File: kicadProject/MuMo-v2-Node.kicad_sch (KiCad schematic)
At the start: 75 parts, among them Q1 PJC7400, SW1 Reset, U1 MCP73123, U2 LoRa-E5, U3 CP2102N, U4 eInk_Display_1.54"200x200px, U5 BME680, U6 TSL25911, U7 BR24G512FVT-5AE2, U8 BR24G512FVT-5AE2

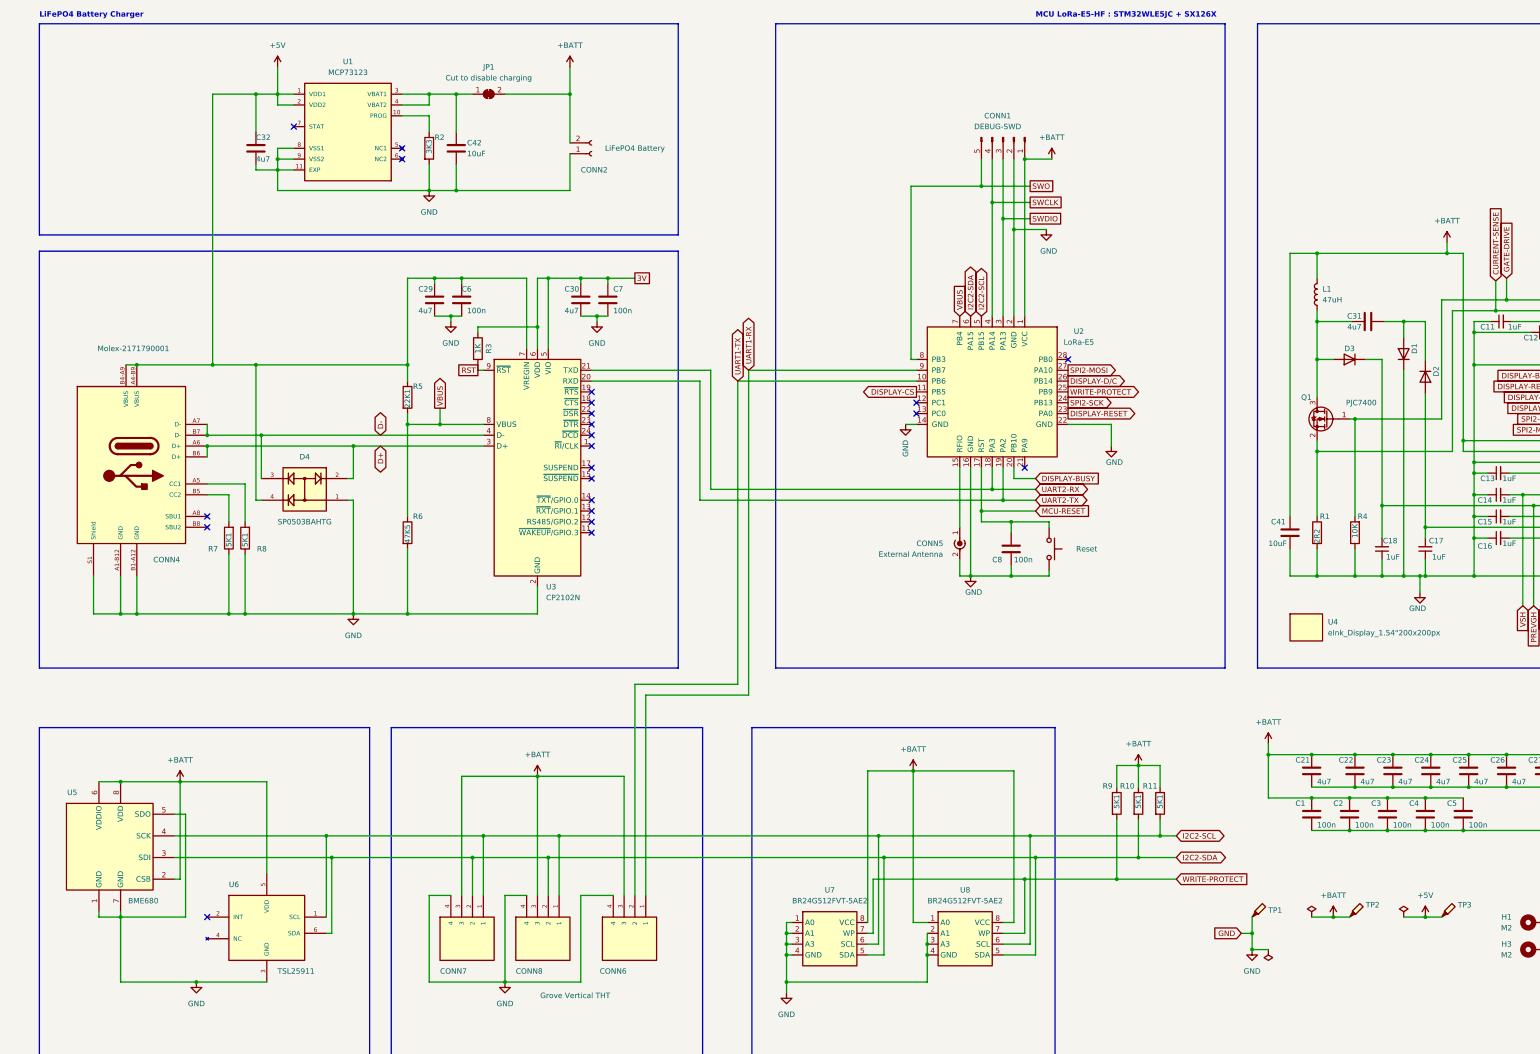
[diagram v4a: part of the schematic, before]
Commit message: V2.4
Updated to Kicad V7
* small design improvements, resolving the DRC of V7
* ready for production at Aisler
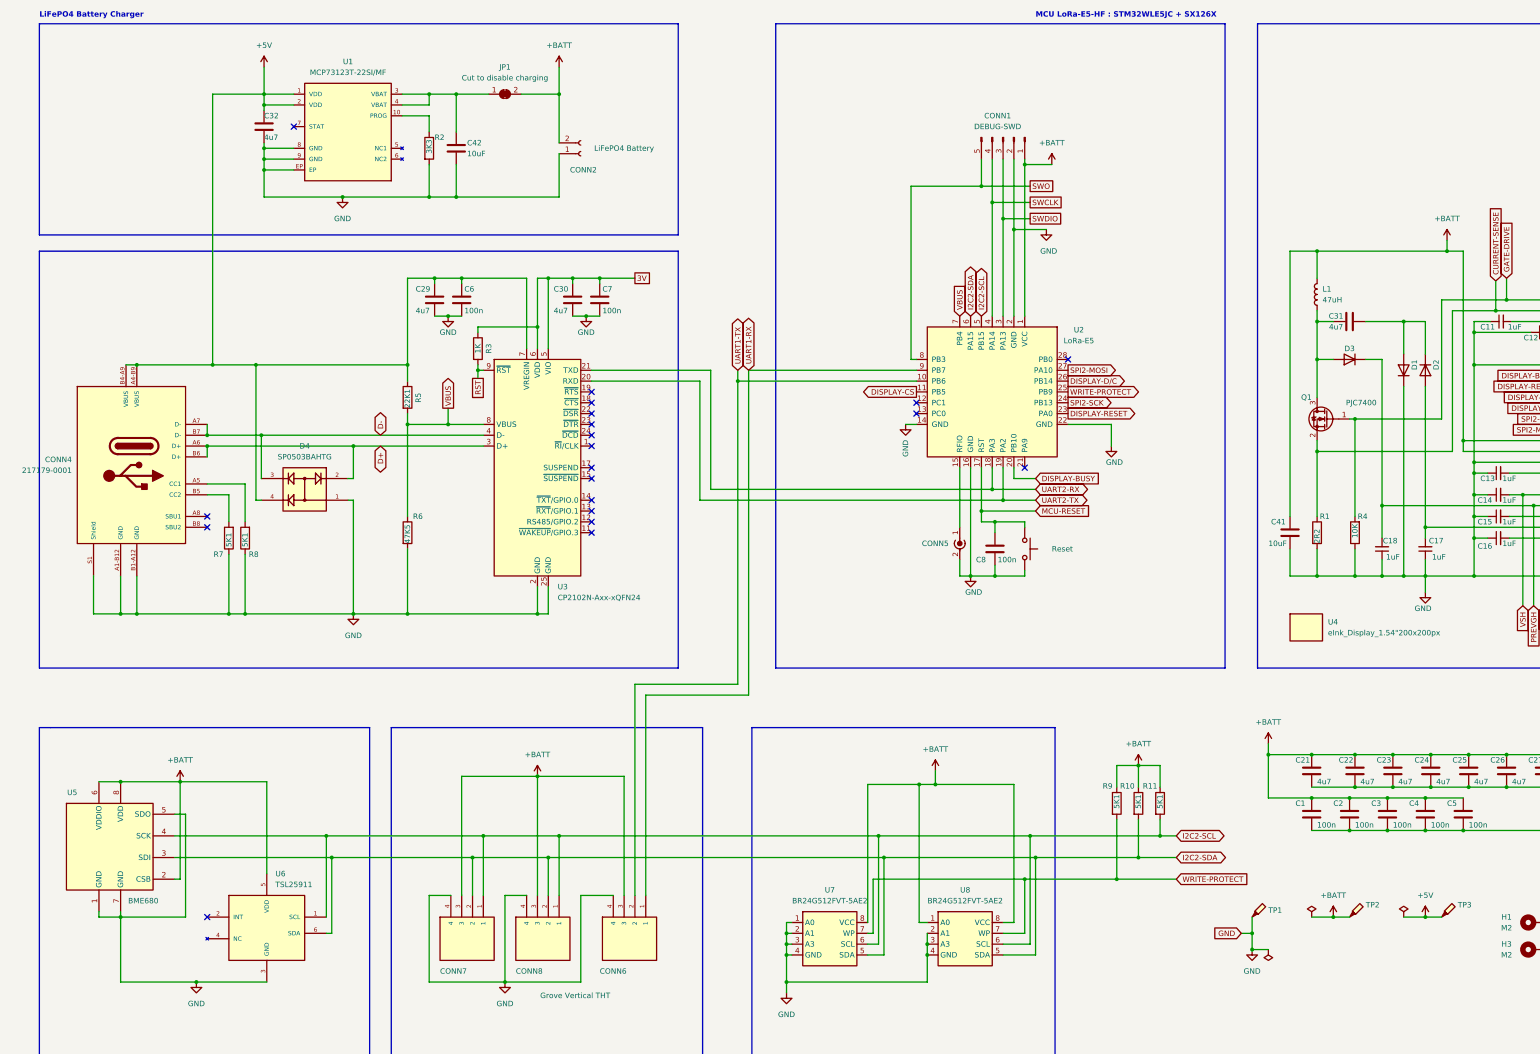
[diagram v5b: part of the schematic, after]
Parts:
- removed U1: MCP73123, thisProjectLibrary:DFN10, symbol thisProjectLibrary:MCP73123T-22SI/MF
- removed U3: CP2102N, thisProjectLibrary:QFN24 - CP2102N, symbol Interface_USB:CP2102N-Axx-xQFN24
- removed U6: TSL25911, thisProjectLibrary:TSL2591-SON, symbol TSL2561:TSL2591
- added U1: MCP73123T-22SI/MF, thisProjectLibrary:DFN10 - MCP73123, symbol thisProjectLibrary:MCP73123T-22SI/MF
- added U3: CP2102N-Axx-xQFN24, thisProjectLibrary:QFN24 - CP2102N, symbol thisProjectLibrary:CP2102N-Axx-xQFN24
- added U6: TSL25911, thisProjectLibrary:TSL2591-SON, symbol thisProjectLibrary:TSL2591
- C1, C2, C3, C5, C6, C7: DESCRIPTION (none) -> Multilayer Ceramic Capacitors MLCC - SMD/SMT CGA 0603 25V 0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; MANUFACTURER (none) -> TDK; MPN (none) -> CGA3E2X7R1E104K080AA; mpn CGA3E2X7R1E104K080AA -> (none)
- C11, C12, C13, C14, C15, C16, C17, C18: DESCRIPTION (none) -> Multilayer Ceramic Capacitors MLCC - SMD/SMT 0603 50VDC 1uF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; MANUFACTURER (none) -> TDK; MPN (none) -> CGA3E1X7R1E105K080AC; mpn CGA3E1X7R1E105K080AC -> (none)
- C21, C23, C24, C25, C26, C29, C30, C31, C32: DESCRIPTION (none) -> Multilayer Ceramic Capacitors MLCC - SMD/SMT 0603 10V 4.7uF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; MANUFACTURER (none) -> TDK; MPN (none) -> C1608X7S1A475K080AC; mpn C1608X7S1A475K080AC -> (none)
- C22, C27, C28: DESCRIPTION (none) -> Multilayer Ceramic Capacitors MLCC - SMD/SMT 0603 10V 4.7uF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; MANUFACTURER (none) -> TDK; MPN (none) -> C1608X7S1A475K080AC; description Multilayer Ceramic Capacitors MLCC - SMD/SMT CGA 0603 25V 0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 -> Multilayer Ceramic Capacitors MLCC - SMD/SMT 0603 10V 4.7uF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; mpn C1608X7S1A475K080AC -> (none); supplier1PartNumber 810-CGA3E2X7R1E104K -> 810-C1608X7S1A475KAC
- C4, C8: DESCRIPTION (none) -> Multilayer Ceramic Capacitors MLCC - SMD/SMT CGA 0603 25V 0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; MANUFACTURER (none) -> TDK; MPN (none) -> CGA3E2X7R1E104K080AA; description Multilayer Ceramic Capacitors MLCC - SMD/SMT 0603 10V 4.7uF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 -> Multilayer Ceramic Capacitors MLCC - SMD/SMT CGA 0603 25V 0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; mpn CGA3E2X7R1E104K080AA -> (none); supplier1PartNumber 810-C1608X7S1A475KAC -> 810-CGA3E2X7R1E104K
- C41, C42: DESCRIPTION (none) -> Multilayer Ceramic Capacitors MLCC - SMD/SMT 0603 10V 10uF 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; MANUFACTURER (none) -> TDK; MPN (none) -> C1608X6S1A106M080AC; PACKAGE 0603 -> (none); mpn C1608X6S1A106M080AC -> (none)
- CONN1: symbol Connector:Conn_01x05_Male -> thisProjectLibrary:DebugPortConnector; DESCRIPTION (none) -> 5-pin Header 2.54mm; MANUFACTURER (none) -> Amphenol FCI; MPN (none) -> 10129378-905002BLF; mpn 10129378-905002BLF -> (none)
- CONN2: symbol Connector:Conn_01x02_Female -> thisProjectLibrary:Connector 2p Battery; DESCRIPTION (none) -> JST XH 2pin THT Vertical; MANUFACTURER (none) -> JST; MPN (none) -> B2B-XH-A (LF)(SN); mpn B2B-XH-A (LF)(SN) -> (none)
- CONN3: symbol Connector_Generic:Conn_01x24 -> thisProjectLibrary:displayConnector 24p FPC; DESCRIPTION (none) -> FFC & FPC connectoren FPC CONN 0.5MM PITCH T/C 24P; MANUFACTURER (none) -> TE Connectivity; MPN (none) -> 2-1734839-4; mpn 2-1734839-4 -> (none)
- CONN4: value Molex-2171790001 -> 217179-0001; DESCRIPTION (none) -> USB Connectors Top-Mnt SMT 16Ckt Type C Rec.; MANUFACTURER (none) -> Molex; MAXIMUM_PACKAGE_HEIGHT 3.31 mm -> (none); MPN (none) -> 217179-0001; STANDARD Manufacturer Recommendations -> (none); description USB-C receptable -> USB Connectors Top-Mnt SMT 16Ckt Type C Rec.; mpn 2171790001 -> (none); package SMT - 16-pin -> (none); stock 18000 -> (none); supplier2Name Digi-Key -> (none); supplier2PartNumber 900-2171790001CT-ND -> (none); supplier2PartURL https://www.digikey.be/nl/products/detail/molex/2171790001/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 -> (none); unitPrice 1.19 -> (none)
- CONN5: value External Antenna -> Conn_Coaxial_Power; DESCRIPTION (none) -> RF Connectors / Coaxial Connectors SMA, Edge Mount, Female 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; MANUFACTURER (none) -> TE Connectivity / Linx Technologies; MPN (none) -> CONSMA020.062-G; description RF-stekkers/Coaxiale stekkers SMA, Edge Mount, Female Recep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 -> RF Connectors / Coaxial Connectors SMA, Edge Mount, Female 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; manufacturer Linx Technologies -> TE Connectivity / Linx Technologies; mpn CONSMA020.062-G -> (none); stock 6400 -> (none); supplier1PartURL https://www.mouser.be/ProductDetail/Linx-Technologies/CONSM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 -> https://www.mouser.be/ProductDetail/TE-Connectivity-Linx-Te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; supplier2Name Digi-Key -> (none); supplier2PartNumber 343-CONSMA020.062-G-ND -> (none); supplier2PartURL https://www.digikey.be/nl/products/detail/linx-technologies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 -> (none); unitPrice 3.93 -> (none)
- CONN6, CONN7, CONN8: footprint thisProjectLibrary:Grove_Vertical -> SEEED_110990030; DESCRIPTION (none) -> Grove THT Vertical PCB Male connector; MANUFACTURER (none) -> Seeed Technology; MAXIMUM_PACKAGE_HEIGHT 8.1mm -> (none); MPN (none) -> 110990030; STANDARD Manufacturer Recommendations -> (none); mpn 110990030 -> (none)
- D1, D2: symbol Device:D -> thisProjectLibrary:D; DESCRIPTION (none) -> Schottky-diodes & gelijkrichters 1.1A .395V; MANUFACTURER (none) -> Vishay Semiconductors; MPN (none) -> SL03-GS08; mpn SL03-GS08 -> (none); supplier2Name Digi-Key -> (none)
- D3: symbol Device:D -> thisProjectLibrary:D; DESCRIPTION (none) -> Schottky-diodes & gelijkrichters 1.1A .395V; MANUFACTURER (none) -> Vishay Semiconductors; MPN (none) -> SL03-GS08; mpn SS1FL3HM3/H -> (none); supplier1PartNumber 78-SS1FL3HM3/H -> 625-SL03
- D4: DESCRIPTION (none) -> ESD Suppressors / TVS Diodes TVS AVAL DIODE SMT; MANUFACTURER (none) -> Littelfuse; MPN (none) -> SP0503BAHTG; PRICE (none) -> 0.46 USD; STANDARD IPC-7351B -> (none); description TVS DIODE 5.5VWM 8.5VC SOT143 -> ESD Suppressors / TVS Diodes TVS AVAL DIODE SMT; mpn SP0503BAHTG -> (none); stock 200000 -> (none); supplier2Name Digi-Key -> Mouser; supplier2PartNumber F2715CT-ND -> (none); supplier2PartURL https://www.digikey.be/nl/products/detail/littelfuse-inc/SP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 -> (none); unitPrice 0.88 -> (none)
- F1, F2, F3: DESCRIPTION (none) -> Fiducial; MANUFACTURER (none) -> notApplicable; MPN (none) -> notApplicable; description (none) -> Fiducial; manufacturer (none) -> notApplicable; mpn notApplicable -> (none); supplier1PartNumber (none) -> notApplicable; supplier1PartURL (none) -> notApplicable
- H1, H2, H3, H4: DESCRIPTION (none) -> Mounting Hole; MANUFACTURER (none) -> notApplicable; MPN (none) -> notApplicable; description (none) -> Mounting Hole; manufacturer (none) -> notApplicable; mpn notApplicable -> (none); supplier1PartNumber (none) -> notApplicable; supplier1PartURL (none) -> notApplicable
- JP1: DESCRIPTION (none) -> Normal Closed PCB Jumper; MANUFACTURER (none) -> notApplicable; MPN (none) -> notApplicable; description (none) -> Normal Closed PCB Jumper; manufacturer (none) -> notApplicable; supplier1Name (none) -> notApplicable; supplier1PartNumber (none) -> notApplicable; supplier1PartURL (none) -> notApplicable
- L1: DESCRIPTION (none) -> Power Inductors - SMD 47uH; MANUFACTURER (none) -> TDK; MPN (none) -> VLS6045EX-470M; mpn VLS6045EX-470M -> (none)
- Q1: DESCRIPTION (none) -> MOSFET 30V Vds 12V Vgs SC70-3; MANUFACTURER (none) -> Panjit; MPN (none) -> PJC7400_R1_00001; mpn PJC7400_R1_00001 -> (none)
- R1: DESCRIPTION (none) -> Current Sense Resistors - SMD 0603 2.2ohm 5% Curr Sense AEC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; MANUFACTURER (none) -> Panasonic; MPN (none) -> ERJ-3RQJ2R2V; mpn ERJ-3RQJ2R2V -> (none)
- R10, R11, R9: DESCRIPTION (none) -> Thick Film Resistors - SMD 0603 5.1KOHMS 5% 1/10WATT; MANUFACTURER (none) -> Bourns; MPN (none) -> CR0603-FX-5101ELF; description Thick Film Resistors - SMD 0603 3.3KOHMS 5% 1/10WATT -> Thick Film Resistors - SMD 0603 5.1KOHMS 5% 1/10WATT; mpn CR0603-FX-5101ELF -> (none); supplier1PartNumber 652-CR0603JW-332EL -> 652-CR0603FX-5101ELF
- R2: DESCRIPTION (none) -> Thick Film Resistors - SMD 0603 3.3KOHMS 5% 1/10WATT; MANUFACTURER (none) -> Bourns; MPN (none) -> CR0603-JW-332ELF; mpn CR0603-JW-332ELF -> (none)
- R3: DESCRIPTION (none) -> Thick Film Resistors - SMD 0603 1KOHMS 5% 1/10WATT; MANUFACTURER (none) -> Bourns; MPN (none) -> CR0603-JW-102ELF; mpn CR0603-JW-102ELF -> (none)
- R4: DESCRIPTION (none) -> Thick Film Resistors - SMD 0603 10KOHMS 5% 1/10WATT; MANUFACTURER (none) -> Bourns; MPN (none) -> CR0603-JW-103ELF; mpn CR0603-JW-103ELF -> (none)
- R5: DESCRIPTION (none) -> Thick Film Resistors - SMD 0603 22.1KOHMS 5% 1/10WATT; MANUFACTURER (none) -> Bourns; MPN (none) -> CR0603-FX-2212ELF; mpn CR0603-FX-2212ELF -> (none)
- R6: DESCRIPTION (none) -> Thick Film Resistors - SMD 0603 47.5KOHMS 5% 1/10WATT; MANUFACTURER (none) -> Bourns; MPN (none) -> CR0603-FX-4752ELF; mpn CR0603-FX-4752ELF -> (none)
- R7, R8: DESCRIPTION (none) -> Thick Film Resistors - SMD 0603 5.1KOHMS 5% 1/10WATT; MANUFACTURER (none) -> Bourns; MPN (none) -> CR0603-FX-5101ELF; mpn CR0603-FX-5101ELF -> (none)
- SW1: DESCRIPTION (none) -> PTS815; MANUFACTURER (none) -> C&K; MPN (none) -> PTS815 SJM 250 SMTR LFS; mpn PTS815 SJM 250 SMTR LFS -> (none)
- TP1, TP2, TP3: DESCRIPTION (none) -> TestPad; MANUFACTURER (none) -> notApplicable; MPN (none) -> notApplicable; description (none) -> TestPad; manufacturer (none) -> notApplicable; mpn notApplicable -> (none); supplier1PartNumber (none) -> notApplicable; supplier1PartURL (none) -> notApplicable
- U2: DESCRIPTION (none) -> Sub-GHz Modules LoRa-E5 Wireless Module; MANUFACTURER (none) -> Seeed Technology; MPN (none) -> 317990687; manufacturer Seeed / ST Microelectronics -> Seeed Technology; mpn 317990687 -> (none); stock 3805 -> (none); supplier2Name Digi-Key -> (none); supplier2PartNumber 1597-317990687-ND -> (none); supplier2PartURL https://www.digikey.be/nl/products/detail/seeed-technology-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 -> (none); unitPrice 9.9 -> (none)
- U4: DESCRIPTION (none) -> ePaper Display; MANUFACTURER (none) -> GoodDisplay; MPN (none) -> GDEH0154D67; mpn GDEH0154D67 -> (none)
- U5: symbol Sensor:BME680 -> thisProjectLibrary:BME680; DESCRIPTION (none) -> Air Quality Sensors MEMS gas, humidity, pressure and temper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; MANUFACTURER (none) -> Bosch Sensortec; MPN (none) -> BME680; mpn BME680 -> (none)
- U7, U8: DESCRIPTION (none) -> EEPROM SERIAL EEPROM; MANUFACTURER (none) -> ROHM; MPN (none) -> BR24G512FVT-5AE2; mpn BR24G512FVT-5AE2 -> (none)
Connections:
- net +5V: now also U1.1 (VDD), U1.2 (VDD), U3.7 (VREGIN)
- net +BATT: now also U6.5 (VDD)
- net 3V: now also U3.5 (VIO), U3.6 (VDD)
- net D+: now also U3.3 (D+)
- net D-: now also U3.4 (D-)
- net GND: now also U1.8 (GND), U1.9 (GND), U1.EP, U3.2 (GND), U3.25 (GND), U6.3 (GND)
- net I2C2-SCL: now also U6.1 (SCL)
- net I2C2-SDA: now also U6.6 (SDA)
- net RST: now also U3.9 (~{RST})
- net UART2-RX: now also U3.21 (TXD)
- net UART2-TX: now also U3.20 (RXD)
- net VBUS: now also U3.8 (VBUS)
- net at C42.1, JP1.1 (A): now also U1.3 (VBAT), U1.4 (VBAT)
- net at R2.1: now also U1.10 (PROG)
- no-connect marks 26 -> 24
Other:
- moved on the sheet: C30, C31, C32, C7, C8, CONN2, D1, D2, JP1
